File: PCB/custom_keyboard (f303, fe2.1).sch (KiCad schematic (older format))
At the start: 448 parts, among them IC1 FE2.1, J2 Conn_01x03_Male, J5 AVR-ISP-6, Q1 DTC123J, SW1 SW_Push, U1 24LC02BT-I/SN, U10 PRTR5V0U2X, U11 XC6206P332MR, U12 74LVC1G34, U13 XC6206P332MR, U14 MIC2505, U15 MIC2505, U2 PRTR5V0U2X, U3 PRTR5V0U2X, U4 PRTR5V0U2X, U5 PRTR5V0U2X, U6 PRTR5V0U2X, U7 PRTR5V0U2X, U8 PRTR5V0U2X, U9 STM32F303CBT6, Y1 8MHz, Y2 32.768KHz, Y3 12MHz

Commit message: Added testpoints to microcontroller
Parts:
- removed TP3: INPUT_GND, symbol Connector:TestPoint
- added D? (x3): Red, LED_SMD:LED_0805_2012Metric, symbol Device:LED_Small
- added D? (x3): Red, symbol Device:LED_Small
- added R? (x6): 330, Resistor_SMD:R_0805_2012Metric, symbol Device:R_Small
- added TP10, TP11, TP12, TP13, TP14, TP15, TP16, TP17, TP18, TP19, TP20, TP21, TP22, TP23, TP24, TP25, TP26, TP27, TP28, TP29, TP30, TP31, TP32, TP33, TP34, TP35, TP36, TP37, TP38, TP39, TP40, TP41, TP42, TP43, TP5, TP6, TP7, TP8, TP9: TestPoint_Small, TestPoint:TestPoint_THTPad_D1.0mm_Drill0.5mm, symbol Connector:TestPoint_Small
- TP1, TP2, TP4: footprint (none) -> TestPoint:TestPoint_THTPad_D1.0mm_Drill0.5mm
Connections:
- net BKL_DATA_IN_3V3: now also TP36.1
- net BOOT0: now also TP22.1
- net COL0: now also TP8.1
- net COL1: now also TP43.1
- net COL10: now also TP34.1
- net COL11: now also TP35.1
- net COL12: now also TP5.1
- net COL13: now also TP6.1
- net COL14: now also TP7.1
- net COL15: now also TP15.1
- net COL16: now also TP16.1
- net COL17: now also TP17.1
- net COL2: now also TP42.1
- net COL3: now also TP41.1
- net COL4: now also TP28.1
- net COL5: now also TP29.1
- net COL6: now also TP30.1
- net COL7: now also TP31.1
- net COL8: now also TP32.1
- net COL9: now also TP33.1
- net ENCODER_A: now also TP18.1
- net ENCODER_B1: now also TP19.1
- net ENCODER_B2: now also TP20.1
- net EXTRA_1: now also TP25.1
- net GND: now also R?.1, R?.1, R?.1, R?.1, R?.1, R?.1
- net HUB_D+: no longer TP2.1
- net HUB_D-: no longer TP1.1
- net KEYBOARD_D+: now also TP40.1
- net KEYBOARD_D-: now also TP39.1
- net KEYBOARD_RESET: now also TP21.1
- net KEYBOARD_SCL: now also TP37.1
- net KEYBOARD_SDA: now also TP38.1
- net KEYBOARD_XTAL1: now also TP23.1
- net KEYBOARD_XTAL2: now also TP24.1
- net PORT1-4_PWR: now also D?.2 (A), D?.2 (A), D?.2 (A)
- net PORT5-7PWR: now also D?.2 (A), D?.2 (A), D?.2 (A)
- net ROT1_ROW: now also TP14.1
- net ROW1: now also TP13.1
- net ROW2: now also TP12.1
- net ROW3: now also TP11.1
- net ROW4: now also TP10.1
- net ROW5: now also TP9.1
- net USB_XTAL1: now also TP26.1
- net USB_XTAL2: now also TP27.1
- net at R2.1, U2.3 (IO2), USB1.5 (DN2)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: now also TP1.1
- net at R4.1, U2.2 (IO1), USB1.6 (DP1)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: now also TP2.1
- new net: D?.1 (K), R?.2 (x6)
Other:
- moved on the sheet: C13, C23, C25, C34, F2, F3, F4, F5, F6, F7, FB10, FB11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

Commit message: connected microcontroller testpoints in PCB
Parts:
- removed TP21, TP22, TP23, TP25: TestPoint_Small, TestPoint:TestPoint_THTPad_D1.0mm_Drill0.5mm, symbol Connector:TestPoint_Small
- added D9: Red, LED_SMD:LED_0805_2012Metric, symbol Device:LED_Small
- added R63: 330, Resistor_SMD:R_0805_2012Metric, symbol Device:R_Small
- added TP3: TestPoint_Small, TestPoint:TestPoint_THTPad_D1.0mm_Drill0.5mm, symbol Connector:TestPoint_Small
- D1, D6, D8: renamed from D?; footprint (none) -> LED_SMD:LED_0805_2012Metric
- gave numbers to parts that had none: 9
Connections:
- net PORT1-4_PWR is gone; now on net +5V: C23.1, C25.1, C34.1, C40.1, D1.2 (A), D4.2 (A), D5.2 (A), F1.1, F1.2, F5.1, F5.2, F6.1, F6.2, F7.1, F7.2, FB10.1, FB10.2, FB11.1, FB11.2, FB15.1, FB15.2, FB9.1, FB9.2, R42.1, U10.4 (VCC), U11.3 (VI), U14.6 (OUT), U14.8 (OUT), U6.4 (VCC), U7.4 (VCC), U8.4 (VCC), USB2.11 (VBUS), USB2.2 (VBUS), USB3.1 (VBUS), USB4.1 (VBUS)
- net +5V: now also D9.2 (A); no longer R15.1, R39.1
- net GND: now also R63.1
- net KEYBOARD_XTAL1: now also TP3.1
- net PORT5-7PWR: now also R15.1, R39.1
- new net: D9.1 (K), R63.2
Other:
- moved on the sheet: FB8, R9

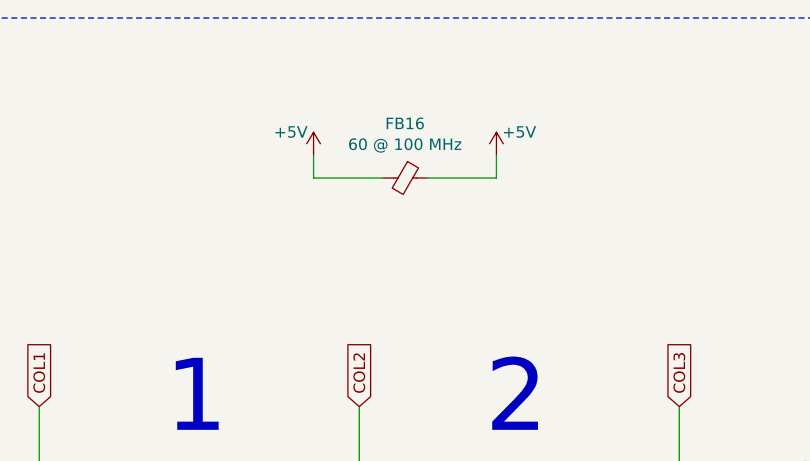
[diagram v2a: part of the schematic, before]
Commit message: Added fuse to LED matrix
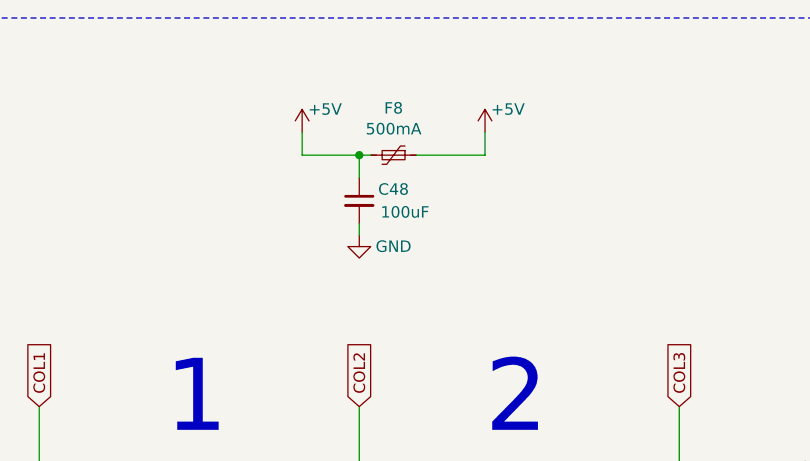
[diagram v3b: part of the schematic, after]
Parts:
- removed FB16: 60 @ 100 MHz, Inductor_SMD:L_0805_2012Metric, symbol Device:Ferrite_Bead_Small
- added C48: 100uF, Capacitor_SMD:C_1206_3216Metric, symbol Device:C_Small
- added F8: 500mA, Fuse:Fuse_1206_3216Metric, symbol Device:Polyfuse_Small
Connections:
- net +5V: now also C48.1, F8.1, F8.2
- net GND: now also C48.2
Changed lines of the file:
@@
 Wire Wire Line
 	4650 21050 4600 21050
-$Comp
-L Device:Ferrite_Bead_Small FB16
-U 1 1 CAF4EC3C
-P 7150 2100
-F 0 "FB16" V 6913 2100 50  0000 C CNN
-F 1 "60 @ 100 MHz" V 7004 2100 50  0000 C CNN
-F 2 "Inductor_SMD:L_0805_2012Metric" V 7080 2100 50  0001 C CNN
-F 3 "~" H 7150 2100 50  0001 C CNN
-	1    7150 2100
-	0    1    1    0
-$EndComp
-$Comp
-L power:+5V #PWR094
-U 1 1 CAF4FFC3
-P 7550 2000
-F 0 "#PWR094" H 7550 1850 50  0001 C CNN
-F 1 "+5V" H 7650 2100 50  0000 C CNN
-F 2 "" H 7550 2000 50  0001 C CNN
-F 3 "" H 7550 2000 50  0001 C CNN
-	1    7550 2000
-	1    0    0    -1
-$EndComp
-$Comp
-L power:+5V #PWR093
-U 1 1 CAF54A00
-P 6750 2000
-F 0 "#PWR093" H 6750 1850 50  0001 C CNN
-F 1 "+5V" H 6850 2100 50  0000 C CNN
-F 2 "" H 6750 2000 50  0001 C CNN
-F 3 "" H 6750 2000 50  0001 C CNN
-	1    6750 2000
-	-1   0    0    -1
-$EndComp
-Wire Wire Line
-	7050 2100 6750 2100
-Wire Wire Line
-	6750 2100 6750 2000
-Wire Wire Line
-	7550 2100 7550 2000
-Wire Wire Line
-	7250 2100 7550 2100
+Wire Wire Line
+	7000 2000 6950 2000
+Wire Wire Line
+	6700 2000 6700 1900
+Wire Wire Line
+	7500 2000 7500 1900
+Wire Wire Line
+	7200 2000 7500 2000
 $Comp
 L Connector:TestPoint TP2
@@
 Wire Wire Line
 	7300 20650 7300 20850
+$Comp
+L power:GND #PWR096
+U 1 1 61F51D49
+P 6950 2350
+F 0 "#PWR096" H 6950 2100 50  0001 C CNN
+F 1 "GND" H 6800 2300 50  0000 C CNN
+F 2 "" H 6950 2350 50  0001 C CNN
+F 3 "" H 6950 2350 50  0001 C CNN
+	1    6950 2350
+	-1   0    0    -1
+$EndComp
+$Comp
+L Device:C_Small C48
+U 1 1 61F55865
+P 6950 2200
+F 0 "C48" H 6800 2250 50  0000 C CNN
+F 1 "100uF" H 6750 2150 50  0000 C CNN
+F 2 "Capacitor_SMD:C_1206_3216Metric" H 6950 2200 50  0001 C CNN
+F 3 "~" H 6950 2200 50  0001 C CNN
+	1    6950 2200
+	-1   0    0    -1
+$EndComp
+Wire Wire Line
+	6950 2350 6950 2300
+Wire Wire Line
+	6950 2100 6950 2000
+Connection ~ 6950 2000
+Wire Wire Line
+	6950 2000 6700 2000
+$Comp
+L Device:Polyfuse_Small F8
+U 1 1 636D2008
+P 7100 2000
+F 0 "F8" V 6895 2000 50  0000 C CNN
+F 1 "500mA" V 6986 2000 50  0000 C CNN
+F 2 "Fuse:Fuse_1206_3216Metric" H 7150 1800 50  0001 L CNN
+F 3 "~" H 7100 2000 50  0001 C CNN
+	1    7100 2000
+	0    1    1    0
+$EndComp
+$Comp
+L power:+5V #PWR?
+U 1 1 6409DD35
+P 6700 1900
+F 0 "#PWR?" H 6700 1750 50  0001 C CNN
+F 1 "+5V" H 6800 2000 50  0000 C CNN
+F 2 "" H 6700 1900 50  0001 C CNN
+F 3 "" H 6700 1900 50  0001 C CNN
+	1    6700 1900
+	1    0    0    -1
+$EndComp
+$Comp
+L power:+5V #PWR?
+U 1 1 6409EAB3
+P 7500 1900
+F 0 "#PWR?" H 7500 1750 50  0001 C CNN
+F 1 "+5V" H 7600 2000 50  0000 C CNN
+F 2 "" H 7500 1900 50  0001 C CNN
+F 3 "" H 7500 1900 50  0001 C CNN
+	1    7500 1900
+	1    0    0    -1
+$EndComp
 $EndSCHEMATC

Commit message: Added JLCPCB Part numbers
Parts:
- removed TP1: HUB_D-, TestPoint:TestPoint_THTPad_D1.0mm_Drill0.5mm, symbol Connector:TestPoint
- removed TP2: HUB_D+, TestPoint:TestPoint_THTPad_D1.0mm_Drill0.5mm, symbol Connector:TestPoint
- removed TP4: EXTRA_1, TestPoint:TestPoint_THTPad_D1.0mm_Drill0.5mm, symbol Connector:TestPoint
- added TP1, TP2, TP4: TestPoint_Small, TestPoint:TestPoint_THTPad_D1.0mm_Drill0.5mm, symbol Connector:TestPoint_Small
- C1, C3: LCSC Part (none) -> C1798
- C10, C13, C2, C23, C25, C34, C48: LCSC Part (none) -> C15008
- C11, C14, C16, C17, C19, C24, C26, C27, C28, C29, C30, C31, C35, C38, C39: LCSC Part (none) -> C49678
- C12, C15, C18: LCSC Part (none) -> C1779
- C20: LCSC Part (none) -> C1710
- C21, C40, C41, C42, C43: LCSC Part (none) -> C28323
- C22, C36, C37, C44, C46, LC1, LC10, LC11, LC12, LC13, LC14, LC15, LC16, LC17, LC18, LC19, LC2, LC20, LC21, LC22, LC23, LC24, LC25, LC26, LC27, LC28, LC29, LC3, LC30, LC31, LC32, LC33, LC34, LC35, LC36, LC37, LC38, LC39, LC4, LC40, LC41, LC42, LC43, LC44, LC45, LC46, LC47, LC48, LC49, LC5, LC50, LC51, LC52, LC53, LC54, LC55, LC56, LC57, LC58, LC59, LC6, LC60, LC61, LC62, LC63, LC64, LC65, LC66, LC67, LC68, LC69, LC7, LC70, LC71, LC72, LC73, LC74, LC75, LC76, LC77, LC78, LC79, LC8, LC80, LC81, LC82, LC83, LC84, LC85, LC86, LC87, LC88, LC89, LC9, LC90: LCSC Part (none) -> C15850
- C32, C33: LCSC Part (none) -> C1804
- C4, C9: LCSC Part (none) -> C1785
- C45, C47, C5, C6, C7, C8: value 0.1uF -> 100nF; LCSC Part (none) -> C49678
- D1, D10, D4, D5, D6, D7, D8, D9: LCSC Part (none) -> C84256
- D2, D3, DRST1, KD1, KD10, KD11, KD12, KD13, KD14, KD15, KD16, KD17, KD18, KD19, KD2, KD20, KD21, KD22, KD23, KD24, KD25, KD26, KD27, KD28, KD29, KD3, KD30, KD31, KD32, KD33, KD34, KD35, KD36, KD37, KD38, KD39, KD4, KD40, KD41, KD42, KD43, KD44, KD45, KD46, KD47, KD48, KD49, KD5, KD50, KD51, KD52, KD53, KD54, KD55, KD56, KD57, KD58, KD59, KD6, KD60, KD61, KD62, KD63, KD64, KD65, KD66, KD67, KD68, KD69, KD7, KD70, KD71, KD72, KD73, KD74, KD75, KD76, KD77, KD78, KD79, KD8, KD80, KD81, KD82, KD83, KD84, KD85, KD86, KD87, KD88, KD89, KD9, KD90: LCSC Part (none) -> C81598
- F1, F2, F3, F4, F5, F6, F7, F8: LCSC Part (none) -> C70069
- FB1, FB10, FB11, FB12, FB13, FB14, FB15, FB2, FB3, FB4, FB5, FB6, FB7, FB8, FB9: LCSC Part (none) -> C18305
- IC1: LCSC Part (none) -> C39693
- J2: LCSC Part (none) -> C160403
- Q1: LCSC Part (none) -> C56452
- R1, R17, R18, R26, R29, R32, R38, R57, R58, R59, R60, R61, R62, R63, R7: LCSC Part (none) -> C17630
- R10, R11, R27, R28, R35, R36, R8, R9: LCSC Part (none) -> C27834
- R12, R13, R14, R15, R39, R40, R48, R49, R50, R51, R52, R53: LCSC Part (none) -> C17414
- R16, R47: LCSC Part (none) -> C17710
- R19, R2, R20, R24, R25, R3, R31, R33, R34, R37, R4, R43, R44, R45, R46, R6: LCSC Part (none) -> C17561
- R21, R23, R30, R54, R55, R56: LCSC Part (none) -> C25803
- R22: LCSC Part (none) -> C17713
- R41: LCSC Part (none) -> C17530
- R42: LCSC Part (none) -> C4310
- R5: LCSC Part (none) -> C17655
- SW1: LCSC Part (none) -> C318884
- TP10, TP11, TP12, TP13, TP14, TP15, TP16, TP17, TP18, TP19, TP20, TP24, TP26, TP27, TP28, TP29, TP3, TP30, TP31, TP32, TP33, TP34, TP35, TP36, TP37, TP38, TP39, TP40, TP41, TP42, TP43, TP5, TP6, TP7, TP8, TP9, USB3, USB4, USB6: JLCPCB BOM (none) -> 0
- U1: LCSC Part (none) -> C511263
- U10, U2, U3, U4, U5, U6, U7, U8: LCSC Part (none) -> C2827688
- U11, U13: LCSC Part (none) -> C5446
- U12: LCSC Part (none) -> C526347
- U14, U15: LCSC Part (none) -> C219158
- U9: LCSC Part (none) -> C108516
- UD1, UD2, UD3, UD4, UD5, UD6, UD7: LCSC Part (none) -> C2297
- USB1, USB2, USB5, USB7: LCSC Part (none) -> C165948
- Y1: LCSC Part (none) -> C367183
- Y2: LCSC Part (none) -> C32346
- Y3: LCSC Part (none) -> C9002
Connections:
- net EXTRA_1: now also TP4.1
- net at R2.1, U2.3 (IO2), USB1.5 (DN2)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: now also TP1.1
- net at R4.1, U2.2 (IO1), USB1.6 (DP1)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: now also TP2.1

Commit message: Minor adjustments to schematic and pcb
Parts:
- added TP21, TP22, TP23, TP25, TP44, TP45, TP46, TP47, TP48, TP49, TP50, TP51, TP52, TP53, TP54: TestPoint_Small, TestPoint:TestPoint_THTPad_D1.0mm_Drill0.5mm, symbol Connector:TestPoint_Small
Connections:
- net +5V: no longer C23.1, C25.1, C34.1, C40.1, D1.2 (A), D4.2 (A), D5.2 (A), D9.2 (A), F1.1, F1.2, F5.1, F5.2, F6.1, F6.2, F7.1, F7.2, FB10.1, FB10.2, FB11.1, FB11.2, FB15.1, FB15.2, FB8.2, FB9.1, FB9.2, R13.1, R42.1, R48.1, U10.4 (VCC), U11.3 (VI), U12.5 (VCC), U14.6 (OUT), U14.8 (OUT), U2.4 (VCC), U6.4 (VCC), U7.4 (VCC), U8.4 (VCC), USB1.11 (VBUS), USB1.2 (VBUS), USB2.11 (VBUS), USB2.2 (VBUS), USB3.1 (VBUS), USB4.1 (VBUS)
- net BKL_DATA_IN: now also TP54.1
- net GND: no longer R61.1
- net PORT5-7PWR: now also TP53.1; no longer C10.1, C13.1, C2.1, D6.2 (A), D7.2 (A), D8.2 (A), F2.1, F2.2, F3.1, F3.2, F4.1, F4.2, FB12.2, FB13.2, FB14.2, U3.4 (VCC), U4.4 (VCC), U5.4 (VCC), USB5.11 (VBUS), USB5.2 (VBUS), USB6.1 (VBUS), USB7.11 (VBUS), USB7.2 (VBUS)
- net at R3.2, U3.3 (IO2), USB5.5 (DN2)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: now also TP46.1
- net at R6.2, U3.2 (IO1), USB5.6 (DP1)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: now also TP47.1
- net at R19.1, U4.2 (IO1), USB7.6 (DP1)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: now also TP51.1
- net at R20.1, U4.3 (IO2), USB7.5 (DN2)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: now also TP50.1
- net at R33.1, U6.2 (IO1), USB2.6 (DP1)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: now also TP25.1
- net at R31.1, U6.3 (IO2), USB2.5 (DN2)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: now also TP23.1
- net at R24.1, U5.2 (IO1), USB6.3 (D+): now also TP48.1
- net at R25.1, U5.3 (IO2), USB6.2 (D-): now also TP49.1
- net at R34.1, U7.2 (IO1), USB3.3 (D+): now also TP21.1
- net at R37.1, U7.3 (IO2), USB3.2 (D-): now also TP22.1
- net at R45.1, U10.2 (IO1), USB4.3 (D+): now also TP44.1
- net at R46.1, U10.3 (IO2), USB4.2 (D-): now also TP45.1
- new net: D9.2 (A), FB8.2, U2.4 (VCC), USB1.11 (VBUS), USB1.2 (VBUS)
- new net: D6.2 (A), F2.2, USB5.11 (VBUS), USB5.2 (VBUS)
- new net: C2.1, F2.1, FB12.2, U3.4 (VCC)
- new net: C10.1, F3.1, FB14.2, U4.4 (VCC)
- new net: D8.2 (A), F3.2, USB7.11 (VBUS), USB7.2 (VBUS)
- new net: C23.1, F5.1, FB10.2, U6.4 (VCC)
- new net: D1.2 (A), F5.2, USB2.11 (VBUS), USB2.2 (VBUS)
- new net: C13.1, F4.2, FB13.2, U5.4 (VCC)
- new net: D5.2 (A), F7.1, USB4.1 (VBUS)
- new net: C34.1, F7.2, FB11.2, U10.4 (VCC)
- new net: D7.2 (A), F4.1, USB6.1 (VBUS)
- new net: C25.1, F6.2, FB9.2, U7.4 (VCC)
- new net: D4.2 (A), F6.1, USB3.1 (VBUS)
- new net VCC: C40.1, F1.1, F1.2, FB10.1, FB11.1, FB15.1, FB15.2, FB9.1, R13.1, R42.1, R48.1, TP52.1, U11.3 (VI), U12.5 (VCC), U14.6 (OUT), U14.8 (OUT), U8.4 (VCC)
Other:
- moved on the sheet: C10, C13, C2, C23, C25, C34, D4, D5, D7, F2, F3, F4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

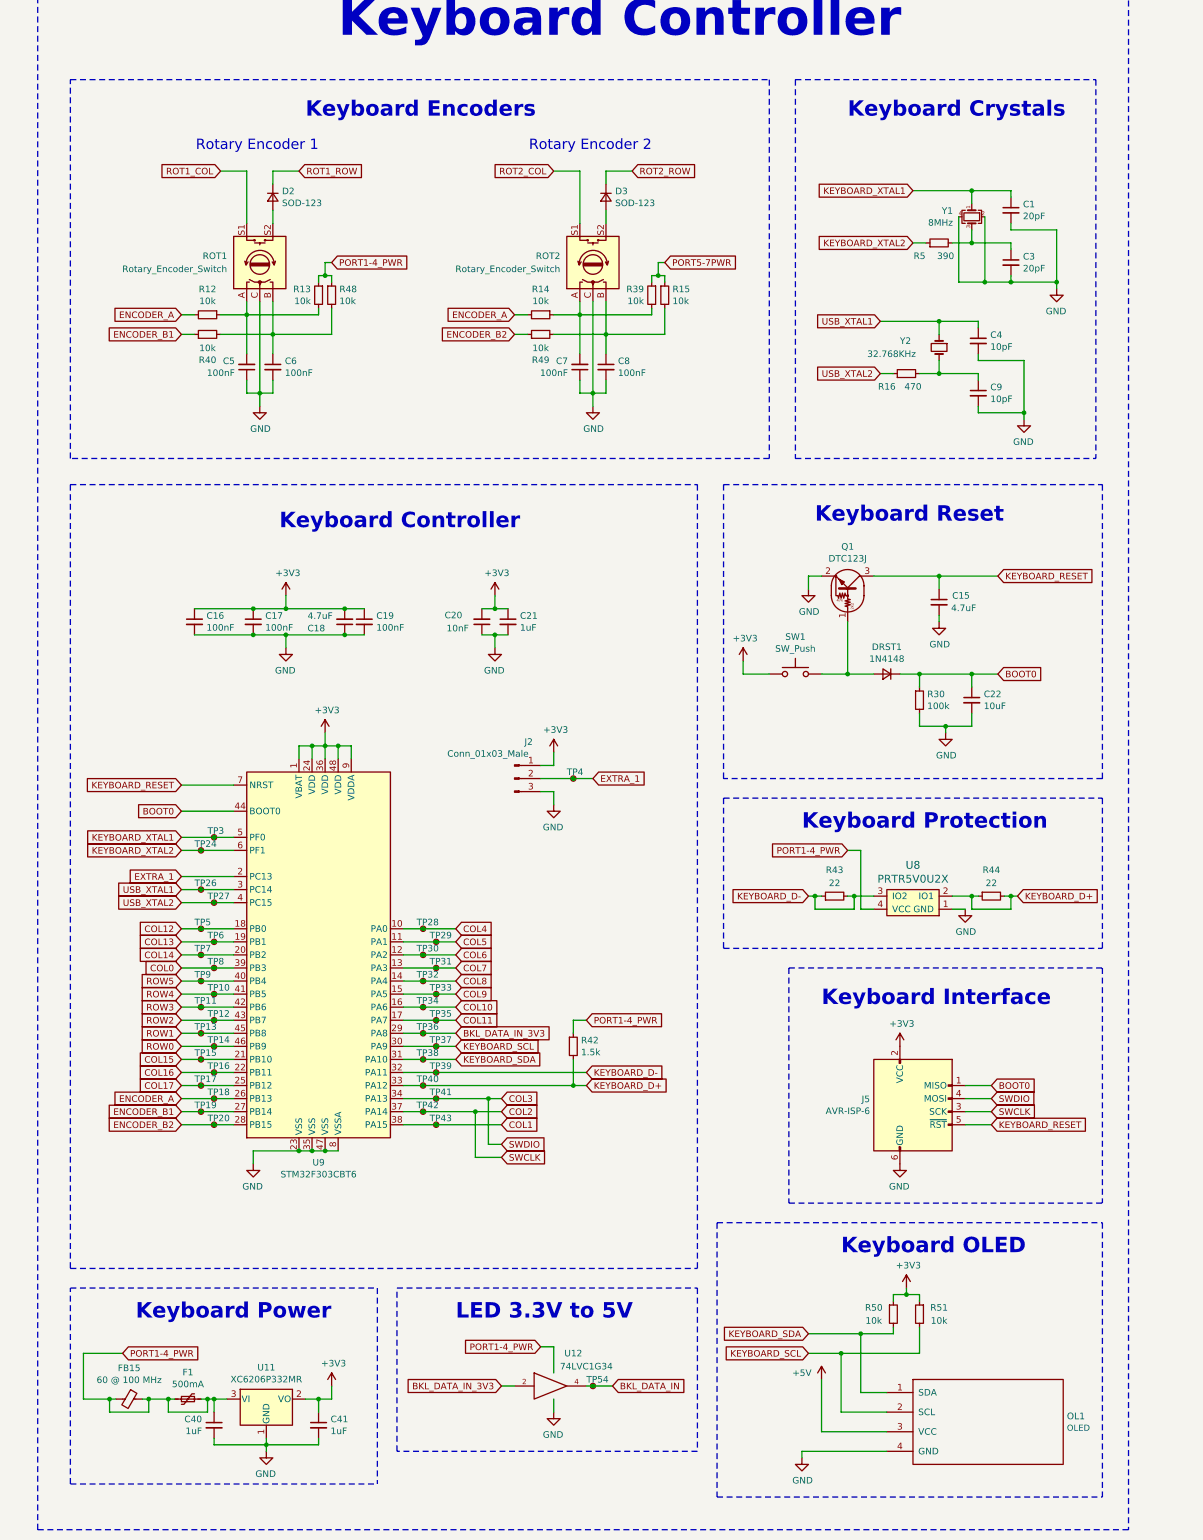
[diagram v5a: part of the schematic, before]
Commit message: Removed pullup resistors on rotary encoders
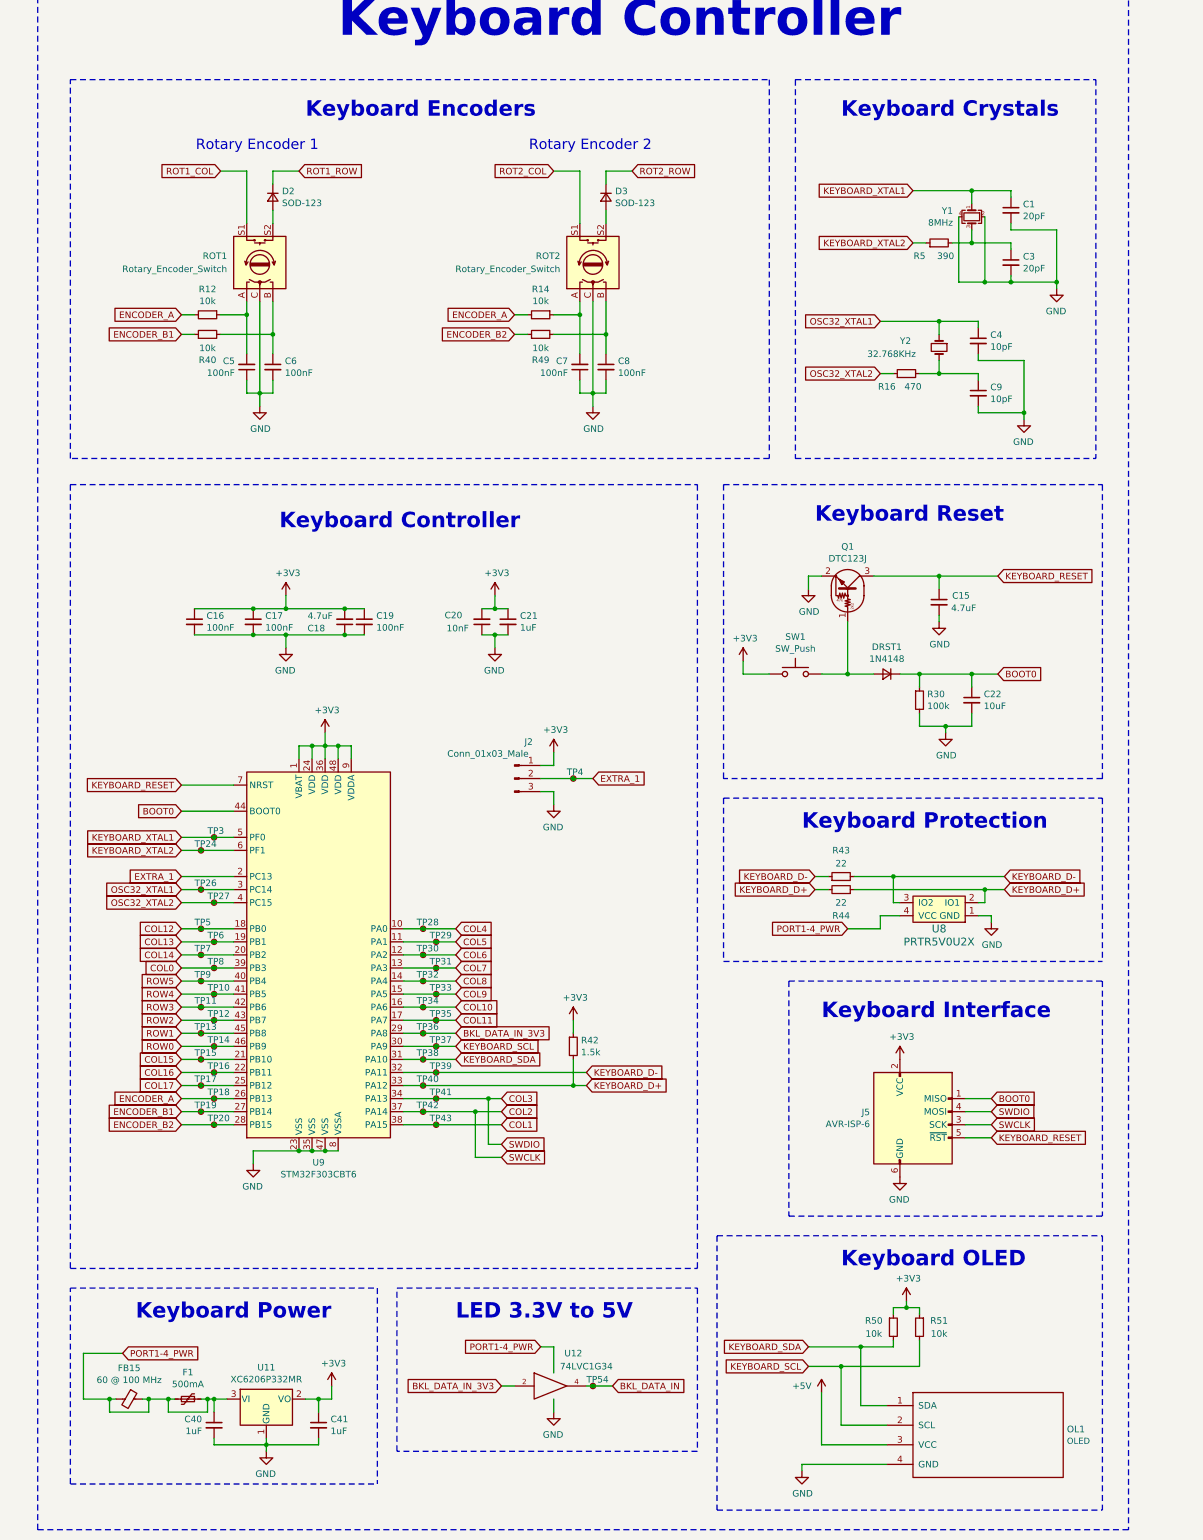
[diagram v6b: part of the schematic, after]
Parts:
- removed R13, R15, R39, R48: 10k, Resistor_SMD:R_0805_2012Metric, symbol Device:R_Small
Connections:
- net +3V3: now also R42.1
- net VCC: no longer R42.1
- net USB_XTAL1 renamed OSC32_XTAL1
- net USB_XTAL2 renamed OSC32_XTAL2
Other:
- moved on the sheet: J5, OL1, R43, R44, R50, R51, U8
